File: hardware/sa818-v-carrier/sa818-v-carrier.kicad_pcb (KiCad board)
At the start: 2 copper layers, 0 parts

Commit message: vhf board layout
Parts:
- added C54: 100nF, Capacitor_SMD:C_0402_1005Metric, F.Cu at (162.8, 65.0)
- added C55: 10uF, Capacitor_SMD:C_0603_1608Metric, F.Cu at (170.9, 65.0)
- added J13: Conn_Coaxial, Connector_Coaxial:SMA_Amphenol_132289_EdgeMount, F.Cu at (140.0, 52.6)
- added J14: Power/Audio, Connector_PinHeader_2.54mm:PinHeader_1x08_P2.54mm_Vertical, F.Cu at (112.0, 87.0)
- added J15: Control/Data, Connector_PinHeader_2.54mm:PinHeader_1x08_P2.54mm_Vertical, F.Cu at (168.0, 87.0)
- added J16: Conn_01x03_Pin, Connector_PinHeader_2.54mm:PinHeader_1x03_P2.54mm_Vertical, F.Cu at (87.0, 53.0)
- added J17: Conn_01x03_Pin, Connector_PinHeader_2.54mm:PinHeader_1x03_P2.54mm_Vertical, F.Cu at (193.0, 53.0)
- added R18: 0, Resistor_SMD:R_0402_1005Metric, F.Cu at (143.0, 87.0)
- added U9: SA818V, VHF_UHF_Modules:VHF_UHF_Module_generic, F.Cu at (140.0, 70.0)
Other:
- board outline added: 120 x 40 mm

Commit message: VHF Carrier Board
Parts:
- moved C55 66.4 mm to (105.6, 76.9), turned to 180 degrees
- moved C54 47.8 mm to (116.5, 76.9), turned to 180 degrees
- moved J13 13.3 mm to (126.7, 52.6)
- turned R18 to 180 degrees
- turned U9 to 180 degrees
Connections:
- J16 pad 3: unconnected-(J16-Pin_3-Pad3) -> GND
- J17 pad 1: unconnected-(J17-Pin_1-Pad1) -> GND
- J17 pad 2: unconnected-(J17-Pin_2-Pad2) -> GND
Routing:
- net Net-(J15-Pin_5): track 0.00 -> 65.5 mm
- net Net-(J15-Pin_6): track 0.00 -> 53.0 mm
- net Net-(J14-Pin_3): track 0.00 -> 47.8 mm
- net Net-(J15-Pin_2): track 0.00 -> 42.1 mm, vias 0 -> 2
- net Net-(J15-Pin_3): track 0.00 -> 41.6 mm
- net Net-(J15-Pin_1): track 0.00 -> 38.4 mm, vias 0 -> 2
- net Net-(J14-Pin_5): track 0.00 -> 30.7 mm, vias 0 -> 2
- net Net-(J14-Pin_1): track 0.00 -> 29.4 mm
- net Net-(J15-Pin_4): track 0.00 -> 16.0 mm
- net Net-(J15-Pin_7): track 0.00 -> 10.2 mm
- net Net-(J13-In): track 0.00 -> 8.60 mm
- net GND: vias 0 -> 8
- added copper zone on B.Cu, net GND
- added copper zone on F.Cu, net GND
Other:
- board text added: "HAM RADIO VILLAGE SSTV BADGE (VHF) SEND ME YOUR MEMES OR POSE FOR A SELFIE JOIN US! https://hamvillage.org"
- board text added: "HRV SSTV BADGE VHF CARRIER BOARD REV 0.1"

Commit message: update text on carrier boards
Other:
- board text added: "HAM RADIO VILLAGE SSTV BADGE (VHF) JOIN US! https://www.hamvillage.org"
- board text added: "HRV SSTV BADGE"
- board text added: "SEND ME UR MEMES!"
- board text added: "VHF CARRIER BOARD Rev 0.1"
- board text removed: "HAM RADIO VILLAGE SSTV BADGE (VHF) SEND ME YOUR MEMES OR POSE FOR A SELFIE JOIN US! https://hamvillage.org"
- board text removed: "HRV SSTV BADGE VHF CARRIER BOARD REV 0.1"
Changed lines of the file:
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@@
 		(layer "Edge.Cuts")
 	)
-	(gr_text "HRV SSTV BADGE\nVHF CARRIER BOARD\nREV 0.1"
-		(at 82.24 87.73 0)
+	(gr_text "HRV SSTV BADGE"
+		(at 80.9752 68.5 0)
 		(layer "F.SilkS")
 		(effects
 			(font
-				(size 1.5 1.5)
-				(thickness 0.1875)
+				(size 3 3)
+				(thickness 0.375)
 			)
 			(justify left bottom)
 		)
 	)
-	(gr_text "HAM RADIO VILLAGE SSTV BADGE (VHF)\nSEND ME YOUR MEMES OR POSE FOR A SELFIE\nJOIN US! https://hamvillage.org"
-		(at 140 76.32 0)
+	(gr_text "SEND ME\nUR MEMES!"
+		(at 173.4632 70.9676 0)
+		(layer "F.SilkS")
+		(effects
+			(font
+				(size 3 3)
+				(thickness 0.375)
+			)
+			(justify left bottom)
+		)
+	)
+	(gr_text "VHF CARRIER BOARD\nRev 0.1"
+		(at 198.6788 87.4776 0)
+		(layer "F.SilkS")
+		(effects
+			(font
+				(size 1 1)
+				(thickness 0.1)
+			)
+			(justify right bottom)
+		)
+	)
+	(gr_text "HAM RADIO VILLAGE SSTV BADGE (VHF)\nJOIN US! https://www.hamvillage.org"
+		(at 139.875 70.1375 0)
 		(layer "B.SilkS")
 		(effects

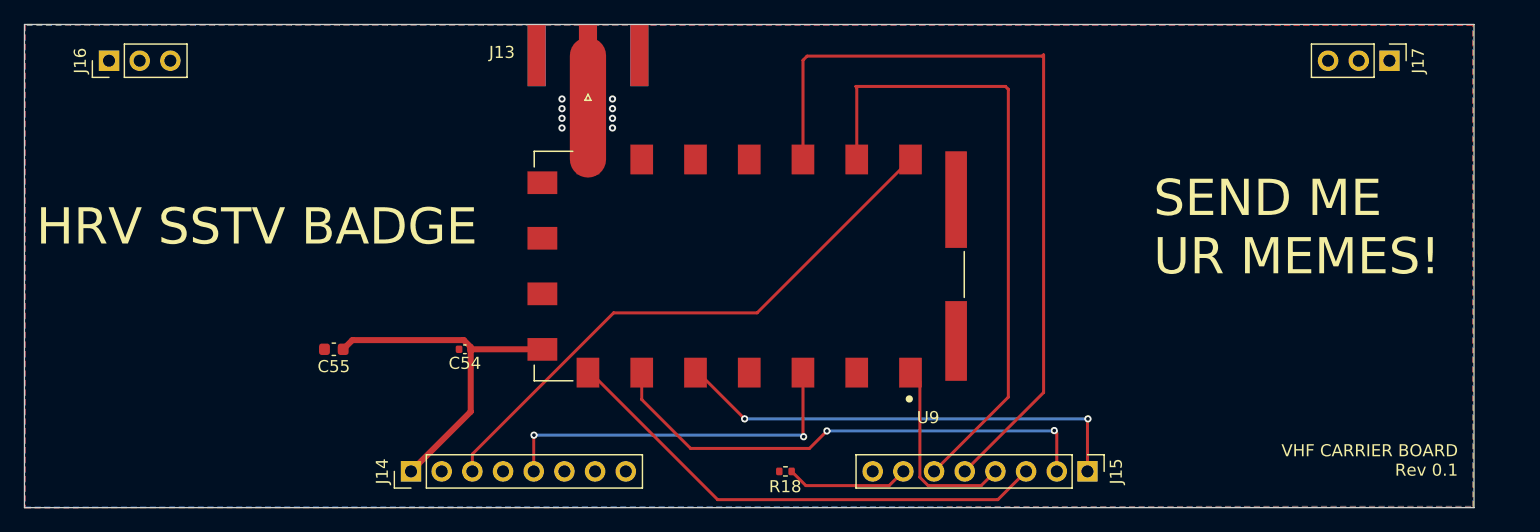
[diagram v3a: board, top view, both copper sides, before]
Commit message: routing and component bug fixes
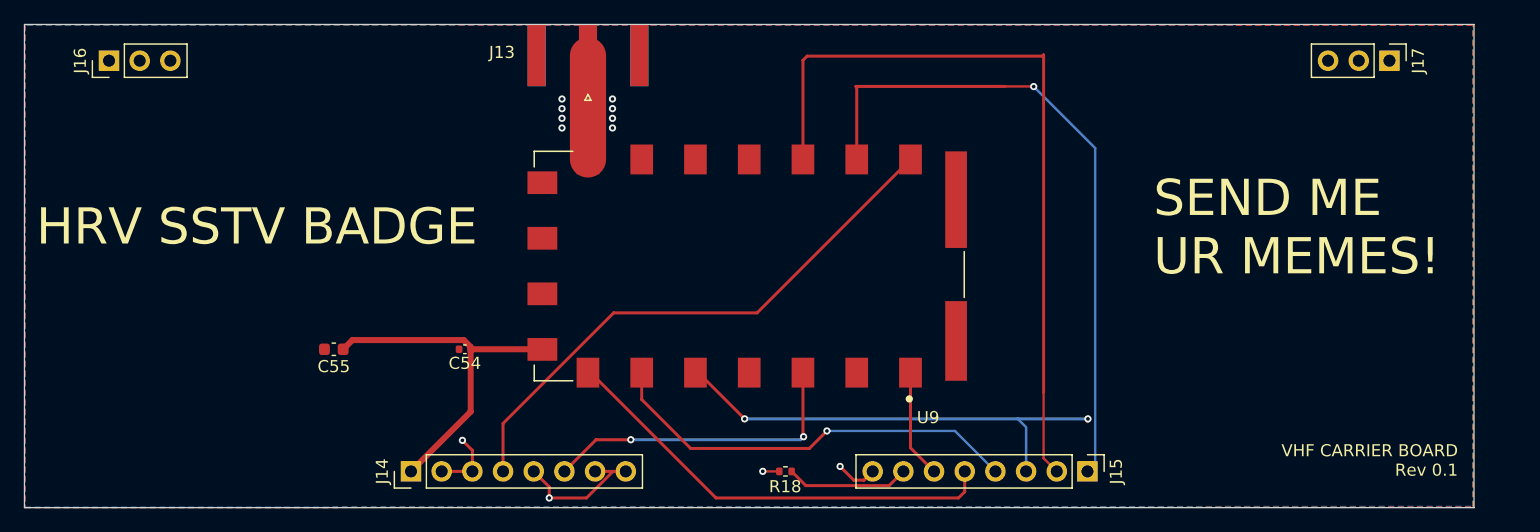
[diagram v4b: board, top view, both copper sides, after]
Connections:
- J14 pad 3: Net-(J14-Pin_3) -> GND
- J14 pad 4: GND -> Net-(J14-Pin_4)
- J14 pad 5: Net-(J14-Pin_5) -> GND
- J14 pad 6: GND -> Net-(J14-Pin_6)
- U9 pad 1: Net-(J15-Pin_4) -> Net-(J15-Pin_6)
- U9 pad 16: Net-(J15-Pin_5) -> Net-(J15-Pin_2)
- U9 pad 17: Net-(J15-Pin_6) -> Net-(J15-Pin_1)
- U9 pad 18: Net-(J14-Pin_3) -> Net-(J14-Pin_4)
- U9 pad 3: Net-(J14-Pin_5) -> Net-(J14-Pin_6)
- U9 pad 5: Net-(J15-Pin_1) -> Net-(J15-Pin_3)
- U9 pad 6: Net-(J15-Pin_2) -> Net-(J15-Pin_4)
- U9 pad 7: Net-(J15-Pin_3) -> Net-(J15-Pin_5)
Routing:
- net Net-(J14-Pin_3): track 47.8 -> 0.00 mm
- net Net-(J14-Pin_4): track 0.00 -> 46.8 mm
- net Net-(J15-Pin_6): track 53.0 -> 10.1 mm
- net Net-(J14-Pin_5): track 30.7 -> 0.00 mm, vias 2 -> 0
- net Net-(J15-Pin_5): track 65.5 -> 37.4 mm
- net Net-(J14-Pin_6): track 0.00 -> 26.5 mm, vias 0 -> 2
- net GND: track 0.00 -> 21.8 mm, vias 8 -> 12
- net Net-(J15-Pin_2): track 42.1 -> 63.2 mm, vias 2 -> 0
- net Net-(J15-Pin_4): track 16.0 -> 35.2 mm, vias 0 -> 1
- net Net-(J15-Pin_1): track 38.4 -> 55.0 mm, vias 2 -> 1
- net Net-(J15-Pin_3): track 41.6 -> 39.0 mm, vias 0 -> 2
